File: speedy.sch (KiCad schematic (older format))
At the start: 41 parts

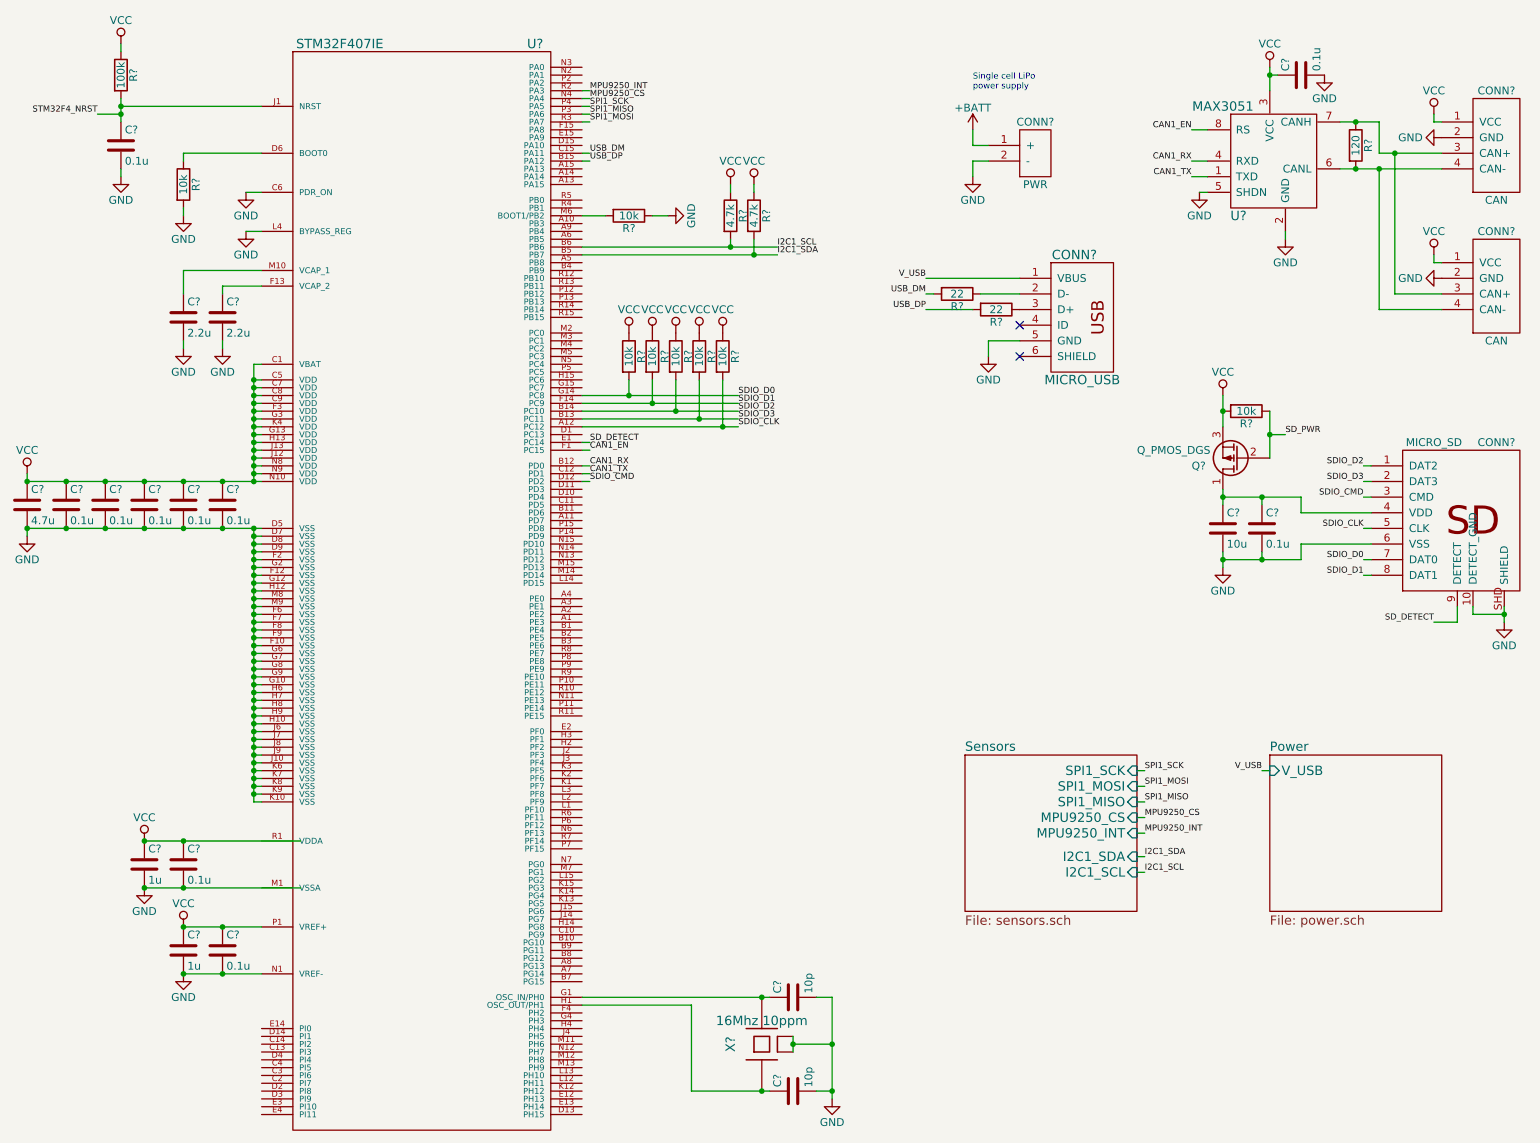
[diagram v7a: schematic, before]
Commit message: Connect motors to timer 1
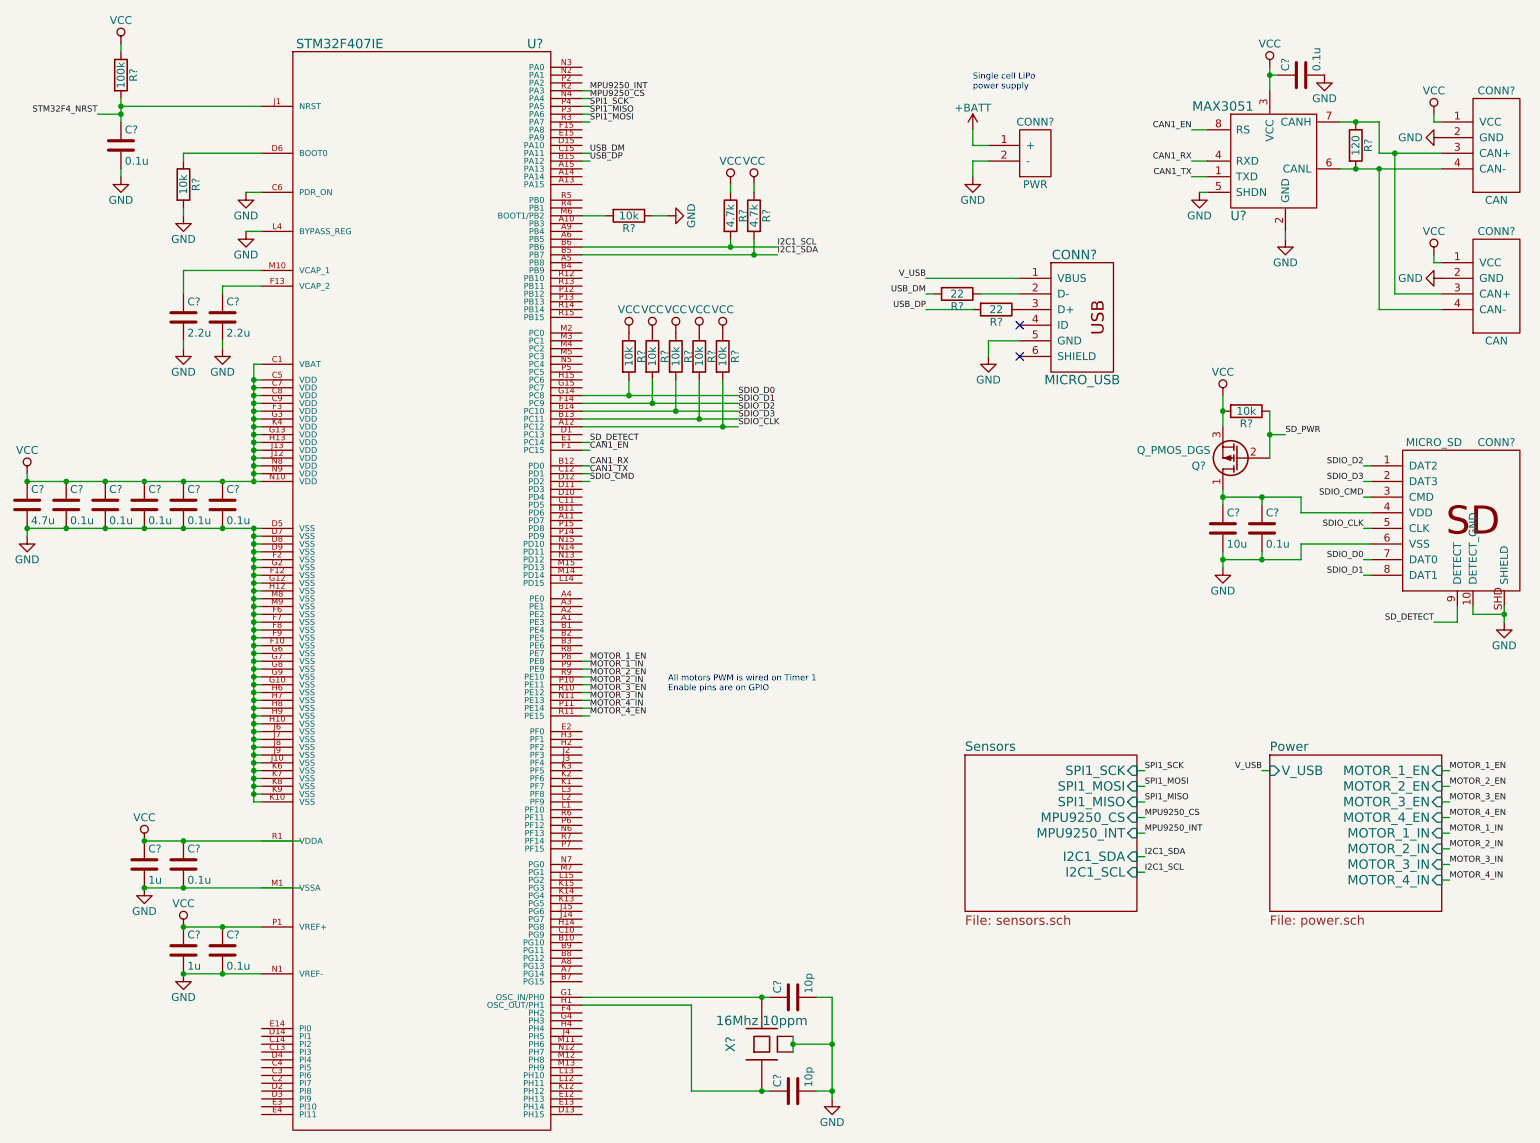
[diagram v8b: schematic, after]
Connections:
- net MOTOR_3_IN: now reaches U?.N11 (PE13)
- net MOTOR_2_IN: now reaches U?.P10 (PE11)
- net MOTOR_4_IN: now reaches U?.P11 (PE14)
- net MOTOR_1_EN: now reaches U?.P8 (PE8)
- net MOTOR_1_IN: now reaches U?.P9 (PE9)
- net MOTOR_3_EN: now reaches U?.R10 (PE12)
- net MOTOR_4_EN: now reaches U?.R11 (PE15)
- net MOTOR_2_EN: now reaches U?.R9 (PE10)
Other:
- note added: "All motors PWM is wired on Timer 1\nEnable pins are on GPIO"
